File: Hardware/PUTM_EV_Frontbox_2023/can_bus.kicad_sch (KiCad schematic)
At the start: 3 parts, among them U5 MCP2542FDxMF

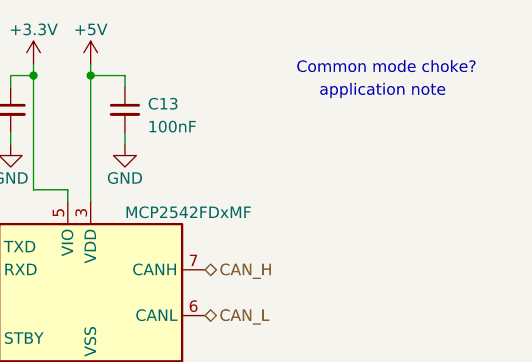
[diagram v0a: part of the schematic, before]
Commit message: Added power section, replaced SWPS
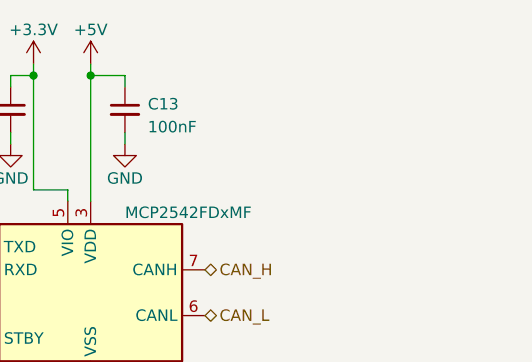
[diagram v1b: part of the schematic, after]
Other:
- note removed: "Common mode choke?"
- note removed: "application note"
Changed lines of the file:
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@@
-    (effects (font (size 1.27 1.27)) (justify left bottom))
-  )
-  (text "Common mode choke?" (at 148.59 88.9 0)
-    (effects (font (size 1.27 1.27)) (justify left bottom))
-  )
-  (text "application note\n" (at 151.13 91.44 0)
     (effects (font (size 1.27 1.27)) (justify left bottom))
   )

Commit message: Schematic ready for review
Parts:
- renumbered C14 to C21, C13 to C22, U5 to U9
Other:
- moved on the sheet: C21, C22, U9

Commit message: Fixed all issues
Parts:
- added FB2: 60R@100MHz, symbol Device:FerriteBead_Small
- added TP2: TestPoint_2Pole, TestPoint:TestPoint_2Pads_Pitch2.54mm_Drill0.8mm, symbol Connector:TestPoint_2Pole
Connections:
- net +5V: now also FB2.1; no longer C22.1, U9.3 (VDD)
- net CAN_RX: now also TP2.2
- net CAN_TX: now also TP2.1
- net GND: now also U9.8 (STBY)
- new net: C22.1, FB2.2, U9.3 (VDD)
- no-connect marks 1 -> 0
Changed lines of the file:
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@@
   (junction (at 142.24 81.28) (diameter 0) (color 0 0 0 0)
   )
-  (no_connect (at 129.54 110.49))
+  (junction (at 142.24 94.615) (diameter 0) (color 0 0 0 0)
+  )
   (wire (pts (xy 139.7 95.25) (xy 139.7 93.98))
     (stroke (width 0) (type default))
@@
     (stroke (width 0) (type default))
   )
+  (wire (pts (xy 142.24 74.295) (xy 142.24 74.93))
+    (stroke (width 0) (type default))
+  )
+  (wire (pts (xy 142.24 94.615) (xy 142.24 95.25))
+    (stroke (width 0) (type default))
+  )
   (wire (pts (xy 133.35 81.28) (xy 135.89 81.28))
     (stroke (width 0) (type default))
@@
     (stroke (width 0) (type default))
   )
-  (wire (pts (xy 142.24 81.28) (xy 142.24 95.25))
+  (wire (pts (xy 160.655 94.615) (xy 160.655 90.805))
+    (stroke (width 0) (type default))
+  )
+  (wire (pts (xy 128.27 111.76) (xy 128.27 110.49))
+    (stroke (width 0) (type default))
+  )
+  (wire (pts (xy 128.27 110.49) (xy 129.54 110.49))
+    (stroke (width 0) (type default))
+  )
+  (wire (pts (xy 142.24 81.28) (xy 142.24 94.615))
     (stroke (width 0) (type default))
   )
   (wire (pts (xy 135.89 80.01) (xy 135.89 81.28))
+    (stroke (width 0) (type default))
+  )
+  (wire (pts (xy 142.24 94.615) (xy 160.655 94.615))
     (stroke (width 0) (type default))
   )
@@
     (effects (font (size 1.27 1.27)) (justify left bottom))
   )
+  (hierarchical_label "CAN_TX" (shape input) (at 179.705 105.41 180) (fields_autoplaced)
+    (effects (font (size 1.27 1.27)) (justify right))
+  )
+  (hierarchical_label "CAN_RX" (shape output) (at 189.865 105.41 0) (fields_autoplaced)
+    (effects (font (size 1.27 1.27)) (justify left))
+  )
   (hierarchical_label "CAN_H" (shape bidirectional) (at 154.94 102.87 0) (fields_autoplaced)
     (effects (font (size 1.27 1.27)) (justify left))
@@
   (hierarchical_label "CAN_TX" (shape input) (at 129.54 100.33 180) (fields_autoplaced)
     (effects (font (size 1.27 1.27)) (justify right))
+  )
+  (symbol (lib_id "Connector:TestPoint_2Pole") (at 184.785 105.41 0) (unit 1)
+    (in_bom yes) (on_board yes) (dnp no)
+    (property "Reference" "TP2" (at 184.785 102.87 0)
+      (effects (font (size 1.27 1.27)))
+    )
+    (property "Value" "TestPoint_2Pole" (at 184.785 102.87 0)
+      (effects (font (size 1.27 1.27)) hide)
+    )
+    (property "Footprint" "TestPoint:TestPoint_2Pads_Pitch2.54mm_Drill0.8mm" (at 184.785 105.41 0)
+      (effects (font (size 1.27 1.27)) hide)
+    )
+    (property "Datasheet" "~" (at 184.785 105.41 0)
+      (effects (font (size 1.27 1.27)) hide)
+    )
+    (pin "1")
+    (pin "2")
+    (instances
+      (project "PUTM_EV_Frontbox_2023"
+        (path "/b652b05a-4e3d-4ad1-b032-18886abe7d45/79afe43e-babf-4d5d-a636-ae8293b09b20"
+          (reference "TP2") (unit 1)
+        )
+        (path "/b652b05a-4e3d-4ad1-b032-18886abe7d45/e2b31807-b5f3-44ae-a974-1e60e93e59ed"
+          (reference "TP3") (unit 1)
+        )
+      )
+    )
   )
   (symbol (lib_id "Device:C_Small") (at 146.05 85.09 0) (unit 1)
@@
   )
   (symbol (lib_id "power:GND") (at 142.24 116.84 0) (unit 1)
+    (in_bom yes) (on_board yes) (dnp no)
+    (property "Reference" "#PWR066" (at 142.24 123.19 0)
+      (effects (font (size 1.27 1.27)) hide)
+    )
+    (property "Value" "GND" (at 142.24 120.65 0)
+      (effects (font (size 1.27 1.27)))
+    )
+    (property "Footprint" "" (at 142.24 116.84 0)
+      (effects (font (size 1.27 1.27)) hide)
+    )
+    (property "Datasheet" "" (at 142.24 116.84 0)
+      (effects (font (size 1.27 1.27)) hide)
+    )
+    (pin "1")
+    (instances
+      (project "PUTM_EV_Frontbox_2023"
+        (path "/b652b05a-4e3d-4ad1-b032-18886abe7d45/e2b31807-b5f3-44ae-a974-1e60e93e59ed"
+          (reference "#PWR066") (unit 1)
+        )
+        (path "/b652b05a-4e3d-4ad1-b032-18886abe7d45/79afe43e-babf-4d5d-a636-ae8293b09b20"
+          (reference "#PWR061") (unit 1)
+        )
+      )
+    )
+  )
+  (symbol (lib_id "power:GND") (at 128.27 111.76 0) (unit 1)
+    (in_bom yes) (on_board yes) (dnp no)
+    (property "Reference" "#PWR0126" (at 128.27 118.11 0)
+      (effects (font (size 1.27 1.27)) hide)
+    )
+    (property "Value" "GND" (at 128.27 115.57 0)
+      (effects (font (size 1.27 1.27)))
+    )
+    (property "Footprint" "" (at 128.27 111.76 0)
+      (effects (font (size 1.27 1.27)) hide)
+    )
+    (property "Datasheet" "" (at 128.27 111.76 0)
+      (effects (font (size 1.27 1.27)) hide)
+    )
+    (pin "1")
+    (instances
+      (project "PUTM_EV_Frontbox_2023"
+        (path "/b652b05a-4e3d-4ad1-b032-18886abe7d45/79afe43e-babf-4d5d-a636-ae8293b09b20"
+          (reference "#PWR0126") (unit 1)
+        )
+        (path "/b652b05a-4e3d-4ad1-b032-18886abe7d45/e2b31807-b5f3-44ae-a974-1e60e93e59ed"
+          (reference "#PWR0127") (unit 1)
+        )
+      )
+    )
+  )
+  (symbol (lib_id "power:PWR_FLAG") (at 160.655 90.805 0) (unit 1)
     (in_bom yes) (on_board yes) (dnp no) (fields_autoplaced)
-    (property "Reference" "#PWR066" (at 142.24 123.19 0)
-      (effects (font (size 1.27 1.27)) hide)
-    )
-    (property "Value" "GND" (at 142.24 121.92 0)
-      (effects (font (size 1.27 1.27)))
-    )
-    (property "Footprint" "" (at 142.24 116.84 0)
-      (effects (font (size 1.27 1.27)) hide)
-    )
-    (property "Datasheet" "" (at 142.24 116.84 0)
-      (effects (font (size 1.27 1.27)) hide)
-    )
-    (pin "1")
-    (instances
-      (project "PUTM_EV_Frontbox_2023"
-        (path "/b652b05a-4e3d-4ad1-b032-18886abe7d45/e2b31807-b5f3-44ae-a974-1e60e93e59ed"
-          (reference "#PWR066") (unit 1)
-        )
-        (path "/b652b05a-4e3d-4ad1-b032-18886abe7d45/79afe43e-babf-4d5d-a636-ae8293b09b20"
-          (reference "#PWR061") (unit 1)
+    (property "Reference" "#FLG08" (at 160.655 88.9 0)
+      (effects (font (size 1.27 1.27)) hide)
+    )
+    (property "Value" "PWR_FLAG" (at 160.655 86.995 0)
+      (effects (font (size 1.27 1.27)))
+    )
+    (property "Footprint" "" (at 160.655 90.805 0)
+      (effects (font (size 1.27 1.27)) hide)
+    )
+    (property "Datasheet" "~" (at 160.655 90.805 0)
+      (effects (font (size 1.27 1.27)) hide)
+    )
+    (pin "1")
+    (instances
+      (project "PUTM_EV_Frontbox_2023"
+        (path "/b652b05a-4e3d-4ad1-b032-18886abe7d45/79afe43e-babf-4d5d-a636-ae8293b09b20"
+          (reference "#FLG08") (unit 1)
+        )
+        (path "/b652b05a-4e3d-4ad1-b032-18886abe7d45/e2b31807-b5f3-44ae-a974-1e60e93e59ed"
+          (reference "#FLG09") (unit 1)
         )
       )
@@
     )
   )
-  (symbol (lib_id "power:+5V") (at 142.24 80.01 0) (unit 1)
+  (symbol (lib_id "power:+5V") (at 142.24 74.295 0) (unit 1)
     (in_bom yes) (on_board yes) (dnp no) (fields_autoplaced)
-    (property "Reference" "#PWR065" (at 142.24 83.82 0)
-      (effects (font (size 1.27 1.27)) hide)
-    )
-    (property "Value" "+5V" (at 142.24 76.2 0)
-      (effects (font (size 1.27 1.27)))
-    )
-    (property "Footprint" "" (at 142.24 80.01 0)
-      (effects (font (size 1.27 1.27)) hide)
-    )
-    (property "Datasheet" "" (at 142.24 80.01 0)
+    (property "Reference" "#PWR065" (at 142.24 78.105 0)
+      (effects (font (size 1.27 1.27)) hide)
+    )
+    (property "Value" "+5V" (at 142.24 70.485 0)
+      (effects (font (size 1.27 1.27)))
+    )
+    (property "Footprint" "" (at 142.24 74.295 0)
+      (effects (font (size 1.27 1.27)) hide)
+    )
+    (property "Datasheet" "" (at 142.24 74.295 0)
       (effects (font (size 1.27 1.27)) hide)
     )
@@
         )
       )
+    )
+  )
+  (symbol (lib_id "Device:FerriteBead_Small") (at 142.24 77.47 0) (unit 1)
+    (in_bom yes) (on_board yes) (dnp no) (fields_autoplaced)
+    (property "Reference" "FB2" (at 144.78 76.7969 0)
+      (effects (font (size 1.27 1.27)) (justify left))
+    )
+    (property "Value" "60R@100MHz" (at 144.78 79.3369 0)
+      (effects (font (size 1.27 1.27)) (justify left))
+    )
+    (property "Footprint" "" (at 140.462 77.47 90)
+      (effects (font (size 1.27 1.27)) hide)
+    )
+    (property "Datasheet" "~" (at 142.24 77.47 0)
+      (effects (font (size 1.27 1.27)) hide)
+    )
+    (pin "1")
+    (pin "2")
+    (instances
+      (project "PUTM_EV_Frontbox_2023"
+        (path "/b652b05a-4e3d-4ad1-b032-18886abe7d45/79afe43e-babf-4d5d-a636-ae8293b09b20"
+          (reference "FB2") (unit 1)
+        )
+        (path "/b652b05a-4e3d-4ad1-b032-18886abe7d45/e2b31807-b5f3-44ae-a974-1e60e93e59ed"
+          (reference "FB3") (unit 1)
+        )
+      )

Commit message: Schematic modified, footprints assigned
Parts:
- C21, C22: footprint (none) -> Capacitor_SMD:C_0402_1005Metric_Pad0.74x0.62mm_HandSolder
- FB2: footprint (none) -> Inductor_SMD:L_0603_1608Metric
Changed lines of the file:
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@@
           (reference "TP2") (unit 1)
         )
-        (path "/b652b05a-4e3d-4ad1-b032-18886abe7d45/e2b31807-b5f3-44ae-a974-1e60e93e59ed"
-          (reference "TP3") (unit 1)
-        )
       )
     )
@@
       (effects (font (size 1.27 1.27)) (justify left))
     )
-    (property "Footprint" "" (at 146.05 85.09 0)
+    (property "Footprint" "Capacitor_SMD:C_0402_1005Metric_Pad0.74x0.62mm_HandSolder" (at 146.05 85.09 0)
       (effects (font (size 1.27 1.27)) hide)
     )
@@
     (instances
       (project "PUTM_EV_Frontbox_2023"
-        (path "/b652b05a-4e3d-4ad1-b032-18886abe7d45/e2b31807-b5f3-44ae-a974-1e60e93e59ed"
-          (reference "C22") (unit 1)
-        )
         (path "/b652b05a-4e3d-4ad1-b032-18886abe7d45/79afe43e-babf-4d5d-a636-ae8293b09b20"
           (reference "C20") (unit 1)
@@
     (instances
       (project "PUTM_EV_Frontbox_2023"
-        (path "/b652b05a-4e3d-4ad1-b032-18886abe7d45/e2b31807-b5f3-44ae-a974-1e60e93e59ed"
-          (reference "#PWR063") (unit 1)
-        )
         (path "/b652b05a-4e3d-4ad1-b032-18886abe7d45/79afe43e-babf-4d5d-a636-ae8293b09b20"
           (reference "#PWR058") (unit 1)
@@
     (instances
       (project "PUTM_EV_Frontbox_2023"
-        (path "/b652b05a-4e3d-4ad1-b032-18886abe7d45/e2b31807-b5f3-44ae-a974-1e60e93e59ed"
-          (reference "#PWR066") (unit 1)
-        )
         (path "/b652b05a-4e3d-4ad1-b032-18886abe7d45/79afe43e-babf-4d5d-a636-ae8293b09b20"
           (reference "#PWR061") (unit 1)
@@
           (reference "#PWR0126") (unit 1)
         )
-        (path "/b652b05a-4e3d-4ad1-b032-18886abe7d45/e2b31807-b5f3-44ae-a974-1e60e93e59ed"
-          (reference "#PWR0127") (unit 1)
-        )
       )
     )
@@
           (reference "#FLG08") (unit 1)
         )
-        (path "/b652b05a-4e3d-4ad1-b032-18886abe7d45/e2b31807-b5f3-44ae-a974-1e60e93e59ed"
-          (reference "#FLG09") (unit 1)
-        )
       )
     )
@@
     (instances
       (project "PUTM_EV_Frontbox_2023"
-        (path "/b652b05a-4e3d-4ad1-b032-18886abe7d45/e2b31807-b5f3-44ae-a974-1e60e93e59ed"
-          (reference "#PWR067") (unit 1)
-        )
         (path "/b652b05a-4e3d-4ad1-b032-18886abe7d45/79afe43e-babf-4d5d-a636-ae8293b09b20"
           (reference "#PWR062") (unit 1)
@@
       (effects (font (size 1.27 1.27)) (justify left))
     )
-    (property "Footprint" "" (at 133.35 85.09 0)
+    (property "Footprint" "Capacitor_SMD:C_0402_1005Metric_Pad0.74x0.62mm_HandSolder" (at 133.35 85.09 0)
       (effects (font (size 1.27 1.27)) hide)
     )
@@
     (instances
       (project "PUTM_EV_Frontbox_2023"
-        (path "/b652b05a-4e3d-4ad1-b032-18886abe7d45/e2b31807-b5f3-44ae-a974-1e60e93e59ed"
-          (reference "C21") (unit 1)
-        )
         (path "/b652b05a-4e3d-4ad1-b032-18886abe7d45/79afe43e-babf-4d5d-a636-ae8293b09b20"
           (reference "C19") (unit 1)
@@
     (instances
       (project "PUTM_EV_Frontbox_2023"
-        (path "/b652b05a-4e3d-4ad1-b032-18886abe7d45/e2b31807-b5f3-44ae-a974-1e60e93e59ed"
-          (reference "#PWR064") (unit 1)
-        )
         (path "/b652b05a-4e3d-4ad1-b032-18886abe7d45/79afe43e-babf-4d5d-a636-ae8293b09b20"
           (reference "#PWR059") (unit 1)
@@
     (instances
       (project "PUTM_EV_Frontbox_2023"
-        (path "/b652b05a-4e3d-4ad1-b032-18886abe7d45/e2b31807-b5f3-44ae-a974-1e60e93e59ed"
-          (reference "U9") (unit 1)
-        )
         (path "/b652b05a-4e3d-4ad1-b032-18886abe7d45/79afe43e-babf-4d5d-a636-ae8293b09b20"
           (reference "U8") (unit 1)
@@
     (instances
       (project "PUTM_EV_Frontbox_2023"
-        (path "/b652b05a-4e3d-4ad1-b032-18886abe7d45/e2b31807-b5f3-44ae-a974-1e60e93e59ed"
-          (reference "#PWR065") (unit 1)
-        )
         (path "/b652b05a-4e3d-4ad1-b032-18886abe7d45/79afe43e-babf-4d5d-a636-ae8293b09b20"
           (reference "#PWR060") (unit 1)
@@
       (effects (font (size 1.27 1.27)) (justify left))
     )
-    (property "Footprint" "" (at 140.462 77.47 90)
+    (property "Footprint" "Inductor_SMD:L_0603_1608Metric" (at 140.462 77.47 90)
       (effects (font (size 1.27 1.27)) hide)
     )
@@
           (reference "FB2") (unit 1)
         )
-        (path "/b652b05a-4e3d-4ad1-b032-18886abe7d45/e2b31807-b5f3-44ae-a974-1e60e93e59ed"
-          (reference "FB3") (unit 1)
-        )
-      )
+      )

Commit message: Grouped components
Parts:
- removed TP2: TestPoint_2Pole, TestPoint:TestPoint_2Pads_Pitch2.54mm_Drill0.8mm, symbol Connector:TestPoint_2Pole
- added TP1, TP2: TestPoint, TestPoint:TestPoint_Pad_1.0x1.0mm, symbol Connector:TestPoint
- renumbered C21 to C19, C22 to C20, U9 to U8
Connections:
- net CAN_RX: now also TP2.1
- net CAN_TX: now also TP1.1

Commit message: routing done
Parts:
- removed TP1, TP2: TestPoint, TestPoint:TestPoint_Pad_1.0x1.0mm, symbol Connector:TestPoint
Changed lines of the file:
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@@
     (effects (font (size 1.27 1.27)) (justify left bottom))
-  )
-  (hierarchical_label "CAN_TX" (shape input) (at 179.705 102.235 180) (fields_autoplaced)
-    (effects (font (size 1.27 1.27)) (justify right))
-  )
-  (hierarchical_label "CAN_RX" (shape output) (at 187.325 102.235 0) (fields_autoplaced)
-    (effects (font (size 1.27 1.27)) (justify left))
   )
   (hierarchical_label "CAN_H" (shape bidirectional) (at 154.94 102.87 0) (fields_autoplaced)
@@
   (hierarchical_label "CAN_TX" (shape input) (at 129.54 100.33 180) (fields_autoplaced)
     (effects (font (size 1.27 1.27)) (justify right))
-  )
-  (symbol (lib_id "Connector:TestPoint") (at 179.705 102.235 0) (unit 1)
-    (in_bom yes) (on_board yes) (dnp no)
-    (property "Reference" "TP1" (at 181.61 98.298 0)
-      (effects (font (size 1.27 1.27)) (justify left))
-    )
-    (property "Value" "TestPoint" (at 181.61 100.838 0)
-      (effects (font (size 1.27 1.27)) (justify left) hide)
-    )
-    (property "Footprint" "TestPoint:TestPoint_Pad_1.0x1.0mm" (at 184.785 102.235 0)
-      (effects (font (size 1.27 1.27)) hide)
-    )
-    (property "Datasheet" "~" (at 184.785 102.235 0)
-      (effects (font (size 1.27 1.27)) hide)
-    )
-    (pin "1")
-    (instances
-      (project "PUTM_EV_Frontbox_2023"
-        (path "/b652b05a-4e3d-4ad1-b032-18886abe7d45/79afe43e-babf-4d5d-a636-ae8293b09b20"
-          (reference "TP1") (unit 1)
-        )
-        (path "/b652b05a-4e3d-4ad1-b032-18886abe7d45/6c790ed6-e097-47bd-81fb-910ea194e2b4"
-          (reference "TP38") (unit 1)
-        )
-      )
-    )
   )
   (symbol (lib_id "Device:C_Small") (at 146.05 85.09 0) (unit 1)
@@
         )
       )
-    )
-  )
-  (symbol (lib_id "Connector:TestPoint") (at 187.325 102.235 0) (unit 1)
-    (in_bom yes) (on_board yes) (dnp no)
-    (property "Reference" "TP2" (at 189.23 98.298 0)
-      (effects (font (size 1.27 1.27)) (justify left))
-    )
-    (property "Value" "TestPoint" (at 189.23 100.838 0)
-      (effects (font (size 1.27 1.27)) (justify left) hide)
-    )
-    (property "Footprint" "TestPoint:TestPoint_Pad_1.0x1.0mm" (at 192.405 102.235 0)
-      (effects (font (size 1.27 1.27)) hide)
-    )
-    (property "Datasheet" "~" (at 192.405 102.235 0)
-      (effects (font (size 1.27 1.27)) hide)
-    )
-    (pin "1")
-    (instances
-      (project "PUTM_EV_Frontbox_2023"
-        (path "/b652b05a-4e3d-4ad1-b032-18886abe7d45/79afe43e-babf-4d5d-a636-ae8293b09b20"
-          (reference "TP2") (unit 1)
-        )
-        (path "/b652b05a-4e3d-4ad1-b032-18886abe7d45/6c790ed6-e097-47bd-81fb-910ea194e2b4"
-          (reference "TP39") (unit 1)
-        )
-      )
